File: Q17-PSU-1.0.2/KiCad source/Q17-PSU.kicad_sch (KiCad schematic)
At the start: 31 parts, among them J1-1 AC1-1, J1-2 AC1-2, J1-3 AC2-1, J1-4 AC2-2, J2-1 V+, J2-2 V+, J2-3 GNDPWR, J2-4 GNDPWR, J2-5 GNDPWR, J2-6 V-, J2-7 V-

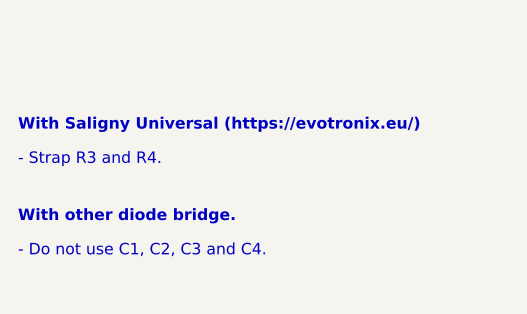
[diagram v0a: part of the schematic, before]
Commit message: Update PSU files to 1.0.2
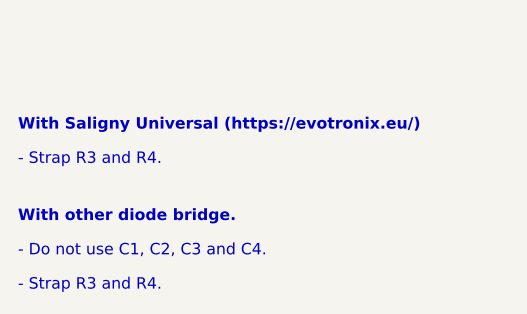
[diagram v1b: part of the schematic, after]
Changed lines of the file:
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@@
   (title_block
     (title "Q17 Power Supply Universal")
-    (date "2023-08-22")
-    (rev "1.0.1")
+    (date "2023-08-27")
+    (rev "1.0.2")
     (company "by stef")
   )
@@
     (effects (font (size 1.27 1.27) (thickness 0.254) bold) (justify left bottom))
   )
+  (text "- Strap R3 and R4." (at 15.24 187.96 0)
+    (effects (font (size 1.27 1.27)) (justify left bottom))
+  )
   (text "- Do not use C1, C2, C3 and C4." (at 15.24 184.15 0)

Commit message: Update PSU files
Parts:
- C1, C2: Mouser 505-MKP1G021002C00KF -> 810-FG28C0G2A103JRT6; Part# MKP1G021002C00KF00 -> FG28C0G2A103JRT06
- C10, C9: footprint Capacitor_THT:C_Rect_L18.0mm_W8.0mm_P15.00mm_FKS3_FKP3 -> Q17_Library:C_Rect_Q17_PSU_L26.50_H11.00_P20.50
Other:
- note added: "C1, C2 : 10nF 100V NPO (COG)"
- note added: "Others capacitors : MKP X2"
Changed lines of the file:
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@@
   (title_block
     (title "Q17 Power Supply Universal")
-    (date "2023-08-27")
-    (rev "1.0.2")
+    (date "2023-08-30")
+    (rev "1.0.3")
     (company "by stef")
   )
@@
     (effects (font (size 1.27 1.27)) (justify left bottom))
   )
+  (text "C1, C2 : 10nF 100V NPO (COG)" (at 83.82 170.18 0)
+    (effects (font (size 1.27 1.27)) (justify left bottom))
+  )
   (text "- Do not use C1, C2, C3 and C4." (at 15.24 184.15 0)
+    (effects (font (size 1.27 1.27)) (justify left bottom))
+  )
+  (text "Others capacitors : MKP X2" (at 83.82 173.99 0)
     (effects (font (size 1.27 1.27)) (justify left bottom))
   )
@@
       (effects (font (size 1.27 1.27)) hide)
     )
-    (property "Datasheet" "https://www.mouser.fr/datasheet/2/440/e_WIMA_MKP_10-1139811.pdf" (at 83.82 77.47 0)
-      (effects (font (size 1.27 1.27)) hide)
-    )
-    (property "Part#" "MKP1G021002C00KF00" (at 83.82 77.47 0)
-      (effects (font (size 1.27 1.27)) hide)
-    )
-    (property "Mouser" "505-MKP1G021002C00KF" (at 83.82 77.47 0)
+    (property "Datasheet" "https://product.tdk.com/system/files/dam/doc/product/capacitor/ceramic/lead-mlcc/catalog/leadmlcc_halogenfree_fg_en.pdf?ref_disty=mouser" (at 83.82 77.47 0)
+      (effects (font (size 1.27 1.27)) hide)
+    )
+    (property "Part#" "FG28C0G2A103JRT06" (at 83.82 77.47 0)
+      (effects (font (size 1.27 1.27)) hide)
+    )
+    (property "Mouser" "810-FG28C0G2A103JRT6" (at 83.82 77.47 0)
       (effects (font (size 1.27 1.27)) hide)
     )
@@
       (effects (font (size 1.27 1.27)) hide)
     )
-    (property "Datasheet" "https://www.mouser.fr/datasheet/2/440/e_WIMA_MKP_10-1139811.pdf" (at 83.82 106.68 0)
-      (effects (font (size 1.27 1.27)) hide)
-    )
-    (property "Part#" "MKP1G021002C00KF00" (at 83.82 106.68 0)
-      (effects (font (size 1.27 1.27)) hide)
-    )
-    (property "Mouser" "505-MKP1G021002C00KF" (at 83.82 106.68 0)
+    (property "Datasheet" "https://product.tdk.com/system/files/dam/doc/product/capacitor/ceramic/lead-mlcc/catalog/leadmlcc_halogenfree_fg_en.pdf?ref_disty=mouser" (at 83.82 106.68 0)
+      (effects (font (size 1.27 1.27)) hide)
+    )
+    (property "Part#" "FG28C0G2A103JRT06" (at 83.82 106.68 0)
+      (effects (font (size 1.27 1.27)) hide)
+    )
+    (property "Mouser" "810-FG28C0G2A103JRT6" (at 83.82 106.68 0)
       (effects (font (size 1.27 1.27)) hide)
     )
@@
       (effects (font (size 1.27 1.27)) (justify left))
     )
-    (property "Footprint" "Capacitor_THT:C_Rect_L18.0mm_W8.0mm_P15.00mm_FKS3_FKP3" (at 180.0352 106.68 0)
+    (property "Footprint" "Q17_Library:C_Rect_Q17_PSU_L26.50_H11.00_P20.50" (at 180.0352 106.68 0)
       (effects (font (size 1.27 1.27)) hide)
     )
@@
       (effects (font (size 1.27 1.27)) (justify left))
     )
-    (property "Footprint" "Capacitor_THT:C_Rect_L18.0mm_W8.0mm_P15.00mm_FKS3_FKP3" (at 180.0352 76.2 0)
-      (effects (font (size 1.27 1.27)) hide)
-    )
+    (property "Footprint" "Q17_Library:C_Rect_Q17_PSU_L26.50_H11.00_P20.50" (at 180.0352 76.2 0)
+      (effects (font (size 1.27 1.27)) hide)
+    )
